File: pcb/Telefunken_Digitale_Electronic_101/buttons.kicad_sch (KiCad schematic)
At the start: 21 parts, among them J1 Conn_01x02_Socket, J2 Conn_01x02_Socket, J3 Conn_01x02_Socket, J4 Conn_01x02_Socket, J5 Conn_01x02_Socket, SW1 SW_Push, SW2 SW_Push

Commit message: SCH - buttons: added footprints to switches (will probably change, need a lower profile)
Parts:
- SW1, SW2: footprint (none) -> Button_Switch_THT:SW_PUSH_6mm_H4.3mm
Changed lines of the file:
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@@
 			)
 		)
-		(property "Footprint" ""
+		(property "Footprint" "Button_Switch_THT:SW_PUSH_6mm_H4.3mm"
 			(at 116.84 34.29 0)
 			(hide yes)
@@
 			)
 		)
-		(property "Footprint" ""
+		(property "Footprint" "Button_Switch_THT:SW_PUSH_6mm_H4.3mm"
 			(at 116.84 58.42 0)
 			(hide yes)

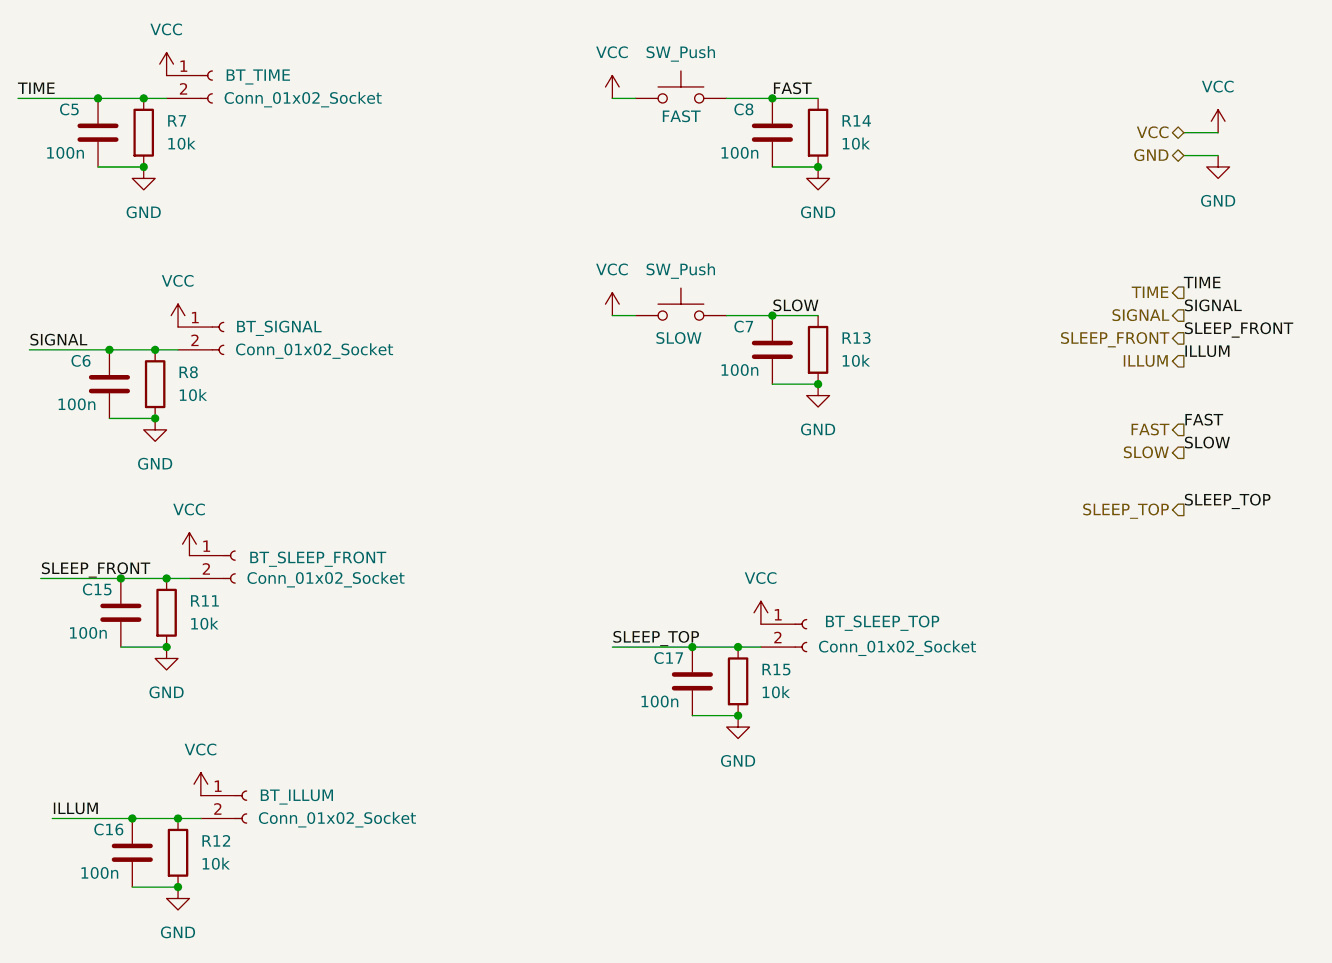
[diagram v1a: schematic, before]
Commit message: SCH - buttons, display and interface: TM1637 can read the buttons (saves many resistors, caps and connectors)
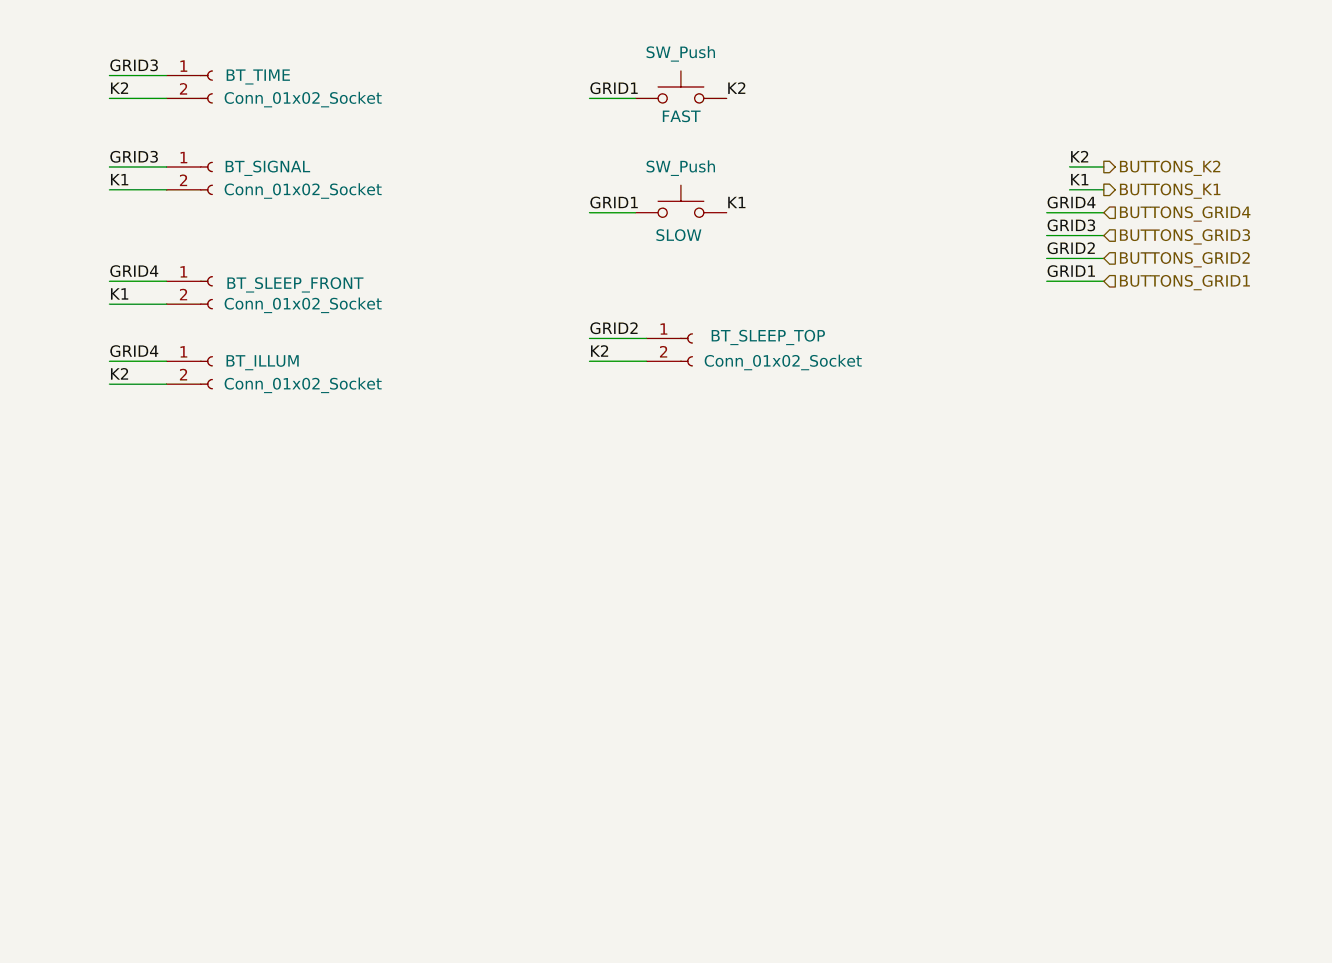
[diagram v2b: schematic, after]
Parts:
- removed C15, C16, C17, C5, C6, C7, C8: 100n, Capacitor_SMD:C_0603_1608Metric_Pad1.08x0.95mm_HandSolder, symbol Device:C
- removed R11, R12, R13, R14, R15, R7, R8: 10k, Resistor_SMD:R_0603_1608Metric_Pad0.98x0.95mm_HandSolder, symbol Device:R
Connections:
- net ILLUM is gone; now on net BUTTONS_K2: J4.2 (Pin_2)
- net SLEEP_FRONT is gone; now on net BUTTONS_K1: J3.2 (Pin_2)
- net SLEEP_TOP is gone; now on net BUTTONS_K2: J5.2 (Pin_2)
- net SLOW is gone; now on net BUTTONS_K1: SW2.2
- net TIME is gone; now on net BUTTONS_K2: J1.2 (Pin_2)
- net FAST renamed BUTTONS_K2
- net SIGNAL renamed BUTTONS_K1
- removed net VCC: J1.1 (Pin_1), J2.1 (Pin_1), J3.1 (Pin_1), J4.1 (Pin_1), J5.1 (Pin_1), SW1.1, SW2.1
- new net BUTTONS_GRID1: SW1.1, SW2.1
- new net BUTTONS_GRID2: J5.1 (Pin_1)
- new net BUTTONS_GRID3: J1.1 (Pin_1), J2.1 (Pin_1)
- new net BUTTONS_GRID4: J3.1 (Pin_1), J4.1 (Pin_1)
